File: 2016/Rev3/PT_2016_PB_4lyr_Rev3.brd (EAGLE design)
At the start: 155.7 x 202.7 mm, 166 parts, among them Q1 Q_IRF7437SMD, Q12 2N7002, Q2 2N7002, Q3 Q_IRF7437SMD

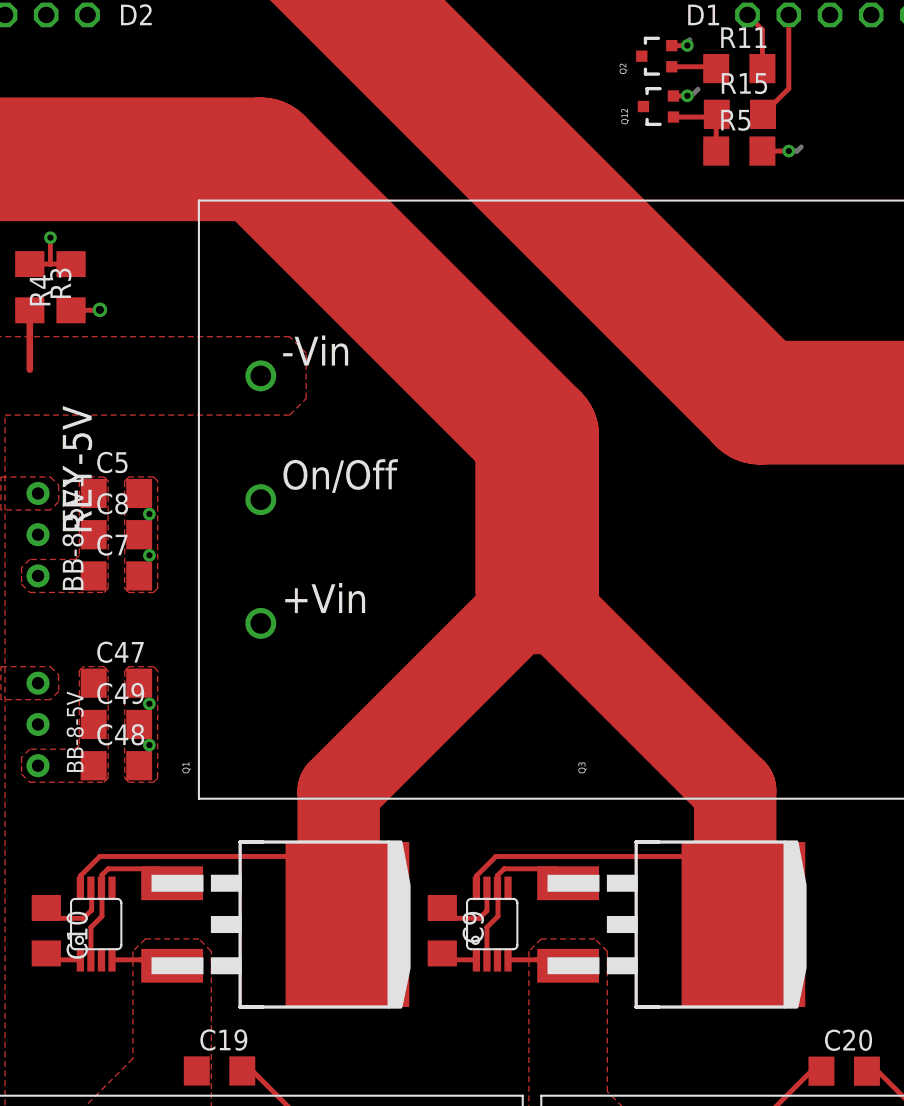
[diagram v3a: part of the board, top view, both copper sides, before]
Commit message: Changed ORing FETs to DPAK
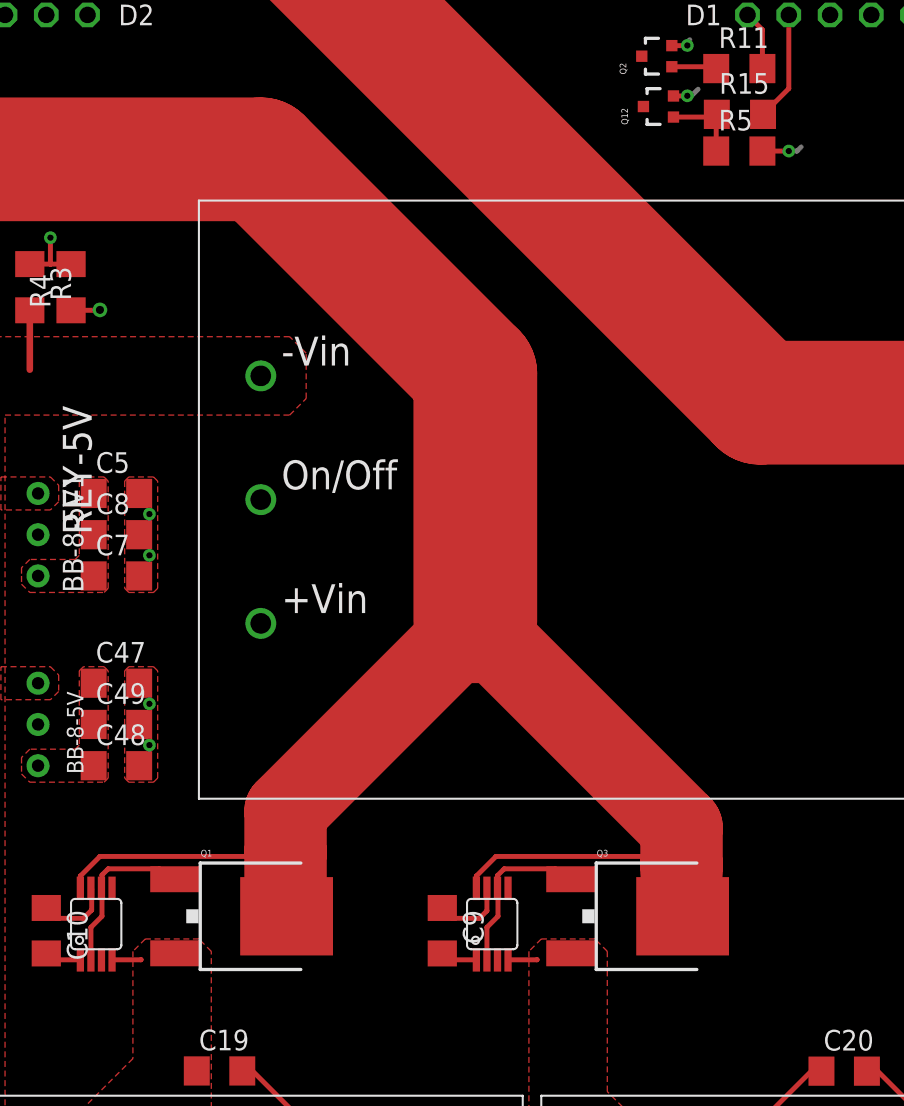
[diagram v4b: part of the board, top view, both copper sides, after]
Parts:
- Q1, Q3: value Q_IRF7437SMD -> MOSFET-NCHANNELFDD8780; device MRDT-2015-PowerBoard:D2PACK -> SparkFun-DiscreteSemi:DPAK
- moved Q1 4.75 mm to (99.8, 97.9)
- moved Q3 4.75 mm to (124.2, 97.9)
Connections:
- net N$1: now also Q3.3; no longer Q3.2
- net N$2: now also Q1.3; no longer Q1.2
- net N$33: now also Q1.4, Q3.4; no longer Q1.TAB, Q3.TAB
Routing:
- net N$33: track 181.3 -> 170.2 mm
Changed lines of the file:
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@@
 <element name="U$9" library="LM74670-Q1" package="LM74670-Q1" value="LM74670-Q1" x="114.046" y="97.536"/>
 <element name="U$13" library="LM74670-Q1" package="LM74670-Q1" value="LM74670-Q1" x="89.662" y="97.536"/>
-<element name="Q1" library="MRDT-2015-PowerBoard" package="D2PACK" value="Q_IRF7437SMD" x="98.552" y="102.489" rot="R270"/>
-<element name="Q3" library="MRDT-2015-PowerBoard" package="D2PACK" value="Q_IRF7437SMD" x="122.936" y="102.489" rot="R270"/>
+<element name="Q1" library="SparkFun-DiscreteSemi" package="DPAK" value="MOSFET-NCHANNELFDD8780" x="99.822" y="97.917" rot="R270">
+<attribute name="PROD_ID" value="TRANS-09984" x="99.822" y="97.917" size="1.778" layer="27" rot="R270" display="off"/>
+</element>
+<element name="Q3" library="SparkFun-DiscreteSemi" package="DPAK" value="MOSFET-NCHANNELFDD8780" x="124.206" y="97.917" rot="R270">
+<attribute name="PROD_ID" value="TRANS-09984" x="124.206" y="97.917" size="1.778" layer="27" rot="R270" display="off"/>
+</element>
 <element name="C9" library="resistor" package="C1206" value="1uF" x="110.998" y="97.028" rot="R270"/>
 <element name="C10" library="resistor" package="C1206" value="1uF" x="86.614" y="97.028" rot="R270"/>
@@
 <wire x1="72.3265" y1="141.70025" x2="79.6925" y2="144.0815" width="0.3048" layer="1"/>
 <wire x1="79.6925" y1="144.0815" x2="79.248" y2="144.526" width="0.3048" layer="1"/>
-<contactref element="Q3" pad="TAB"/>
+<contactref element="Q3" pad="4"/>
 <contactref element="U$9" pad="P$1"/>
-<contactref element="Q1" pad="TAB"/>
+<contactref element="Q1" pad="4"/>
 <contactref element="U$13" pad="P$1"/>
-<wire x1="127" y1="101.6" x2="127.254" y2="101.346" width="0.3048" layer="1"/>
-<wire x1="127.254" y1="101.346" x2="127.254" y2="99.282" width="0.3048" layer="1"/>
-<wire x1="127.254" y1="99.282" x2="129.54" y2="97.409" width="0.3048" layer="1"/>
-<wire x1="99.822" y1="144.526" x2="116.84" y2="127.508" width="7.62" layer="1"/>
-<wire x1="116.84" y1="127.508" x2="116.84" y2="117.856" width="7.62" layer="1"/>
-<wire x1="116.84" y1="117.856" x2="104.616" y2="105.632" width="5.08" layer="1"/>
-<wire x1="114.3" y1="101.6" x2="127" y2="101.6" width="0.3048" layer="1"/>
+<wire x1="99.822" y1="144.526" x2="113.03" y2="131.318" width="7.62" layer="1"/>
+<wire x1="113.03" y1="131.318" x2="113.03" y2="116.078" width="7.62" layer="1"/>
+<wire x1="113.03" y1="116.078" x2="101.346" y2="104.394" width="5.08" layer="1"/>
+<wire x1="101.346" y1="104.394" x2="101.346" y2="101.854" width="5.08" layer="1"/>
+<wire x1="101.346" y1="101.854" x2="101.346" y2="99.06" width="5.08" layer="1"/>
+<wire x1="101.346" y1="99.06" x2="101.41" y2="98.996" width="3.048" layer="1"/>
+<wire x1="101.41" y1="98.996" x2="101.41" y2="97.917" width="3.048" layer="1"/>
+<wire x1="88.712" y1="99.636" x2="88.712" y2="100.396" width="0.3048" layer="1"/>
+<wire x1="88.712" y1="100.396" x2="89.916" y2="101.6" width="0.3048" layer="1"/>
+<wire x1="89.916" y1="101.6" x2="101.092" y2="101.6" width="0.3048" layer="1"/>
+<wire x1="101.092" y1="101.6" x2="101.346" y2="101.854" width="0.3048" layer="1"/>
 <wire x1="113.096" y1="99.636" x2="113.096" y2="100.396" width="0.3048" layer="1"/>
 <wire x1="113.096" y1="100.396" x2="114.3" y2="101.6" width="0.3048" layer="1"/>
-<wire x1="127" y1="101.6" x2="128.778" y2="101.6" width="0.3048" layer="1"/>
-<wire x1="128.778" y1="101.6" x2="129.032" y2="101.346" width="0.3048" layer="1"/>
-<wire x1="129.032" y1="101.346" x2="129.032" y2="105.664" width="5.08" layer="1"/>
-<wire x1="129.032" y1="105.664" x2="116.84" y2="117.856" width="5.08" layer="1"/>
-<wire x1="104.616" y1="105.632" x2="104.616" y2="101.6" width="5.08" layer="1"/>
-<wire x1="104.616" y1="101.6" x2="104.616" y2="97.949" width="5.08" layer="1"/>
-<wire x1="104.616" y1="97.949" x2="105.156" y2="97.409" width="5.08" layer="1"/>
-<wire x1="88.712" y1="99.636" x2="88.712" y2="100.396" width="0.3048" layer="1"/>
-<wire x1="88.712" y1="100.396" x2="89.916" y2="101.6" width="0.3048" layer="1"/>
-<wire x1="89.916" y1="101.6" x2="104.616" y2="101.6" width="0.3048" layer="1"/>
+<wire x1="125.73" y1="100.584" x2="125.73" y2="101.092" width="5.08" layer="1"/>
+<wire x1="125.73" y1="101.092" x2="125.73" y2="103.378" width="5.08" layer="1"/>
+<wire x1="125.73" y1="103.378" x2="113.03" y2="116.078" width="5.08" layer="1"/>
+<wire x1="114.3" y1="101.6" x2="124.968" y2="101.6" width="0.3048" layer="1"/>
+<wire x1="124.968" y1="101.6" x2="124.968" y2="98.743" width="0.3048" layer="1"/>
+<wire x1="124.968" y1="98.743" x2="125.794" y2="97.917" width="0.3048" layer="1"/>
+<wire x1="124.968" y1="101.6" x2="125.222" y2="101.6" width="0.3048" layer="1"/>
+<wire x1="125.222" y1="101.6" x2="125.73" y2="101.092" width="0.3048" layer="1"/>
 </signal>
 <signal name="REC+1">
@@
 <signal name="N$1">
 <contactref element="FINN-12V" pad="8"/>
-<contactref element="Q3" pad="2"/>
+<contactref element="Q3" pad="3"/>
 <contactref element="U$9" pad="P$8"/>
 <contactref element="C20" pad="1"/>
@@
 <signal name="N$2">
 <contactref element="POE-12V" pad="8"/>
-<contactref element="Q1" pad="2"/>
+<contactref element="Q1" pad="3"/>
 <contactref element="U$13" pad="P$8"/>
 <contactref element="C19" pad="1"/>
@@
 <wire x1="114.396" y1="100.426" x2="114.808" y2="100.838" width="0.3048" layer="1"/>
 <wire x1="114.808" y1="100.838" x2="117.963" y2="100.838" width="0.3048" layer="1"/>
-<wire x1="117.963" y1="100.838" x2="118.745" y2="99.949" width="0.3048" layer="1"/>
+<wire x1="117.963" y1="100.838" x2="118.896" y2="100.197" width="0.3048" layer="1"/>
 </signal>
 <signal name="N$5">
@@
 <wire x1="90.043" y1="100.457" x2="90.424" y2="100.838" width="0.3048" layer="1"/>
 <wire x1="90.424" y1="100.838" x2="93.579" y2="100.838" width="0.3048" layer="1"/>
-<wire x1="93.579" y1="100.838" x2="94.361" y2="99.949" width="0.3048" layer="1"/>
+<wire x1="93.579" y1="100.838" x2="94.512" y2="100.197" width="0.3048" layer="1"/>
 <wire x1="89.362" y1="95.236" x2="89.362" y2="97.236" width="0.3048" layer="1"/>
 <wire x1="89.362" y1="97.236" x2="90.043" y2="97.917" width="0.3048" layer="1"/>

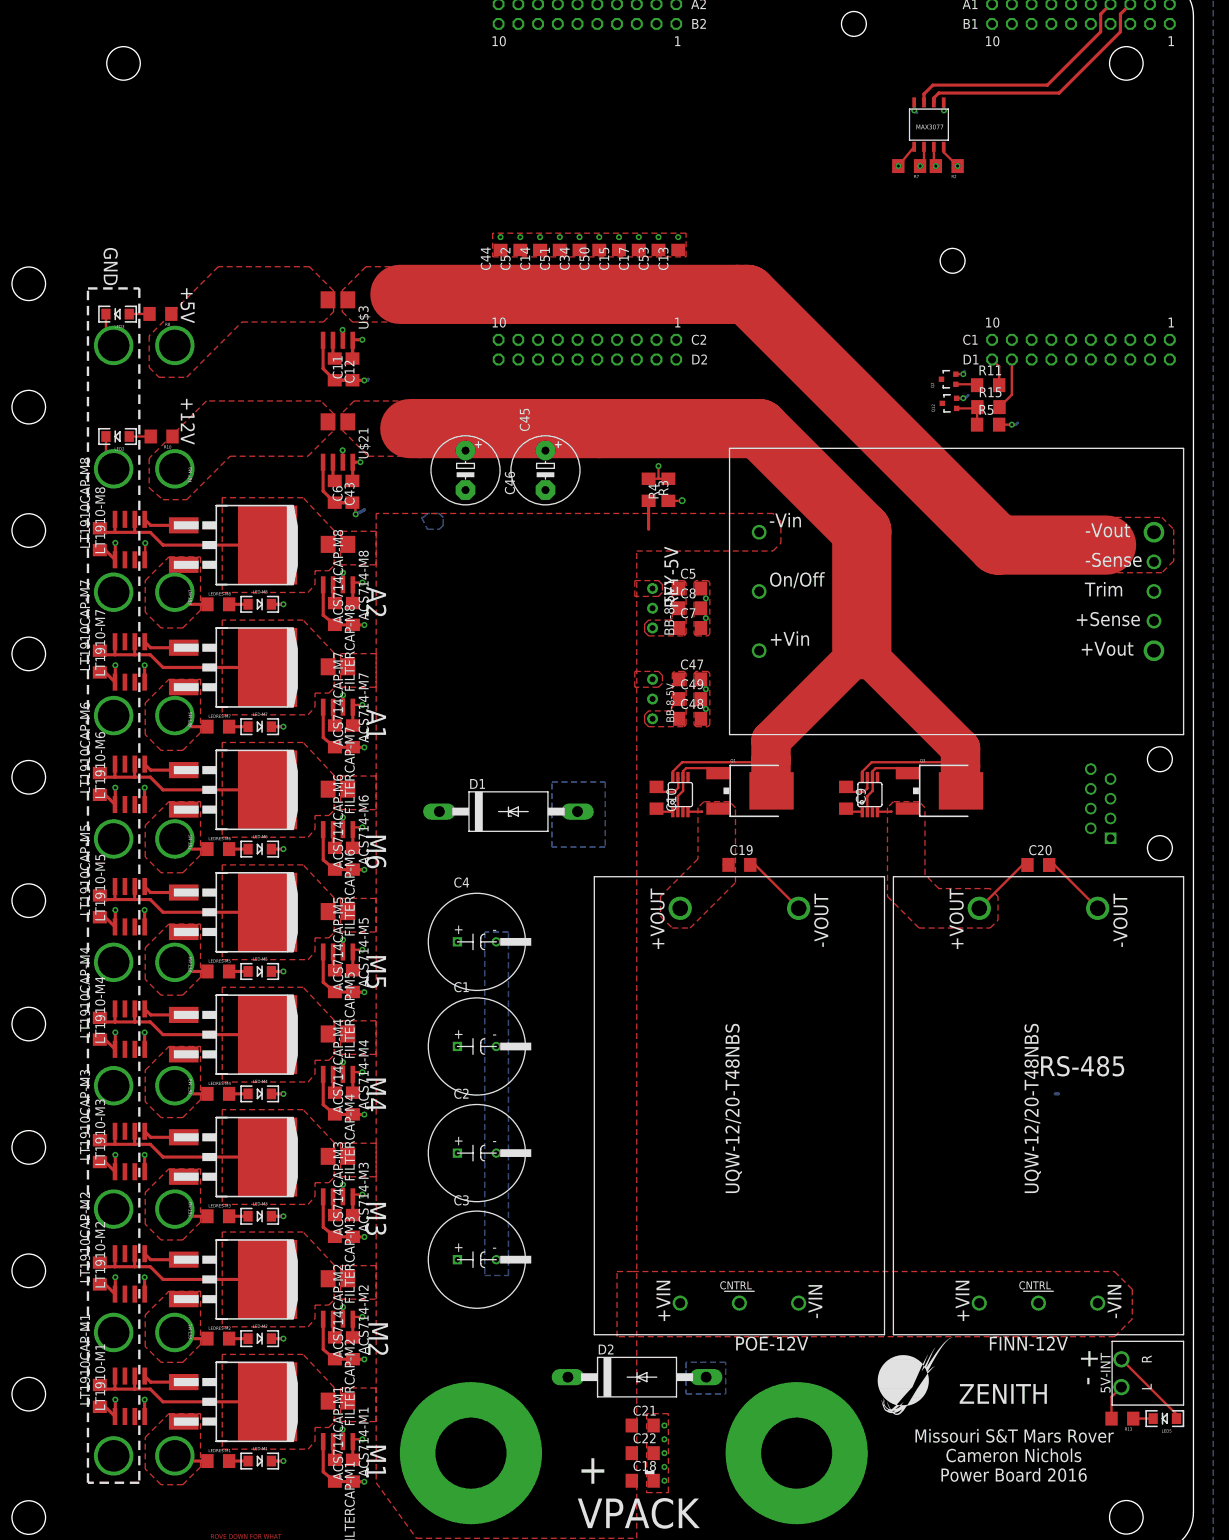
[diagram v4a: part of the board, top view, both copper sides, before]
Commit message: Routed, moved some motor fets over
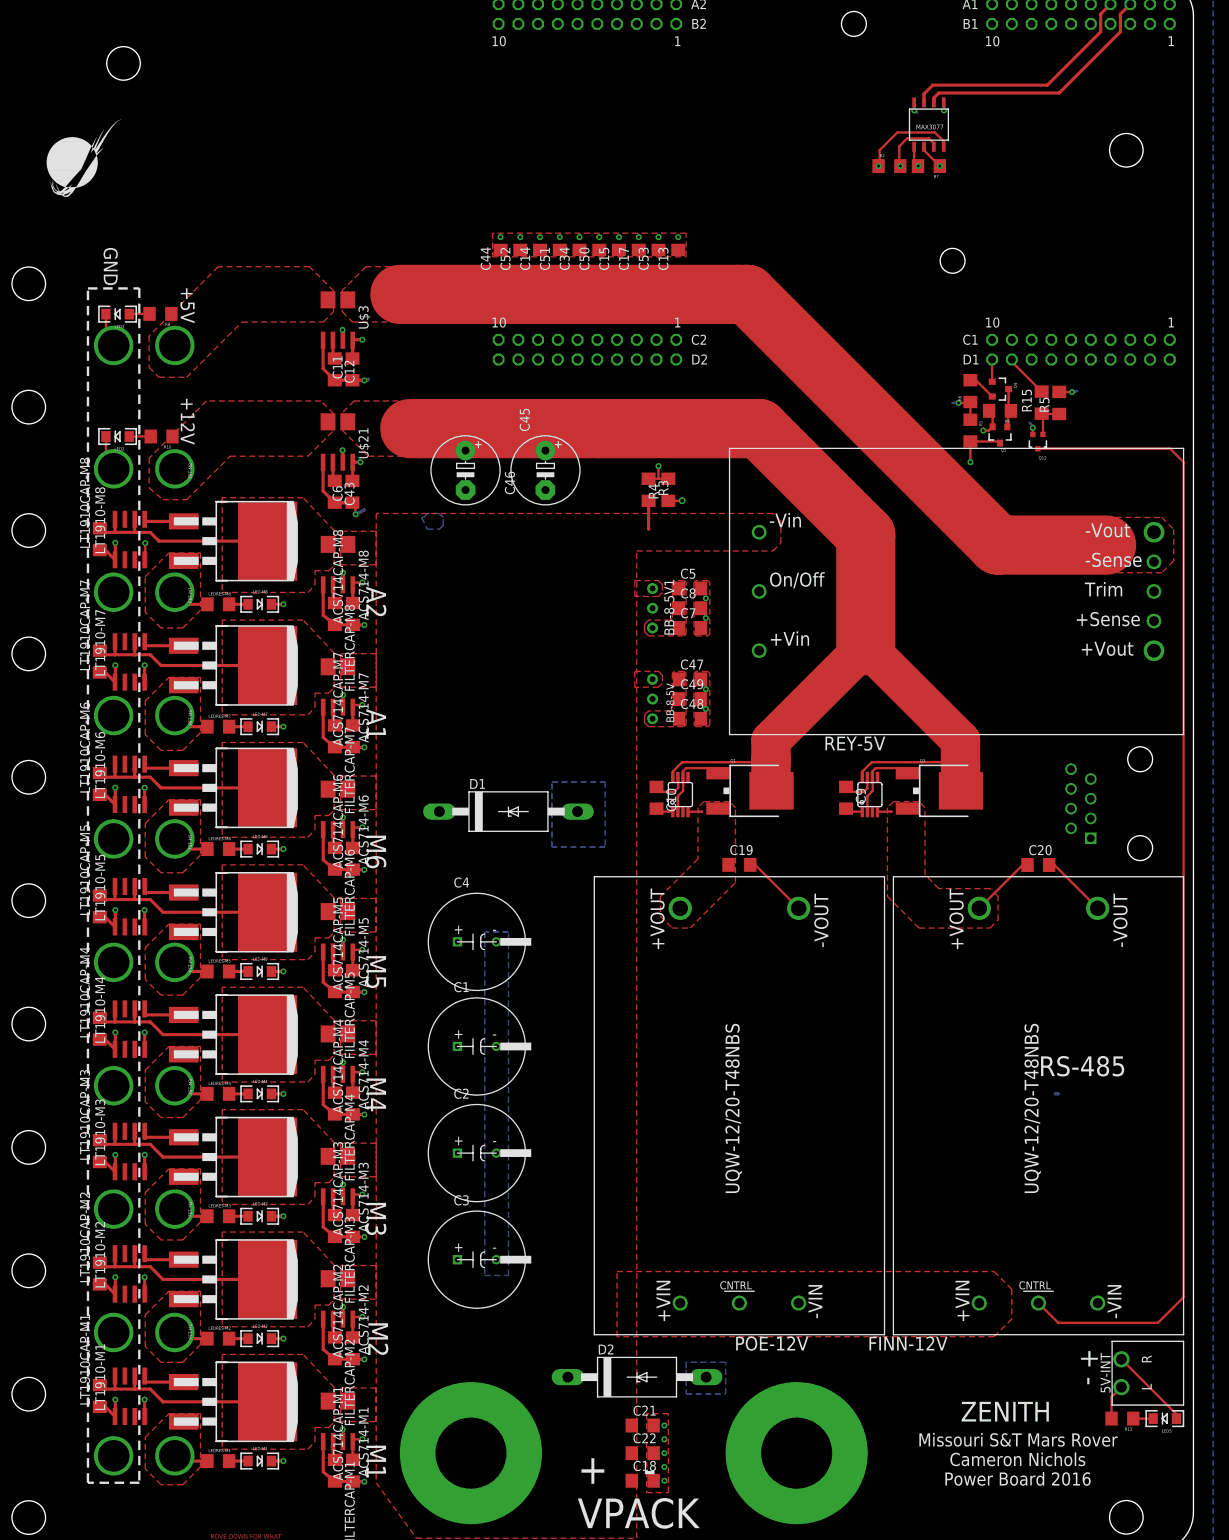
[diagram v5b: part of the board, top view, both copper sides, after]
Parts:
- removed Q2: 2N7002, SparkFun-DiscreteSemi:SOT323
- removed R11: 1k, resistor:R1206
- added Q4: MMBT2222A, SparkFun-DiscreteSemi:SOT23-3
- added Q5: MMBT4403, SparkFun-DiscreteSemi:SOT23-3
- added R1, R6, R9: 120 Ohm, SparkFun-Passives:1206
- moved U$22 189.7 mm to (8.13, 173.5)
- moved Q12 12.4 mm to (135.7, 142.8), turned to 180 degrees
- moved U$11 11.2 mm to (147.1, 180.3)
- moved R5 9.56 mm to (138.4, 147.8), turned to 90 degrees
- moved R2 7.37 mm to (116.6, 178.3), turned to 0 degrees
- moved R15 6.87 mm to (136.2, 147.9), turned to 90 degrees
- moved R7 2.54 mm to (121.7, 178.3)
- moved U$5 2.54 mm to (148.8, 96.3)
- moved FET-M8 0.51 mm to (30.0, 135.1)
- moved FET-M6 0.25 mm to (30.0, 103.4)
- moved FET-M7 0.25 mm to (30.0, 119.1)
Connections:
- removed net N$48: Q2.1, R11.1
- new net N$11: Q4.3, Q5.1, R9.1
- new net N$15: Q4.2, R6.2
- net GND: now also R1.1, R6.1; no longer Q2.2
- net N$43: now also Q5.3, R1.2; no longer Q2.3
- net SIG-5V: now also Q4.1; no longer R11.2
- net V_BATT: now also Q5.2, R9.2
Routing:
- net N$4: track 0.00 -> 188.4 mm
- net N$43: track 0.00 -> 40.6 mm, vias 0 -> 1
- net V_BATT: track 3.66 -> 41.6 mm, vias 0 -> 1
- net TRANS-1: track 104.4 -> 99.0 mm
- net N$11: track 0.00 -> 5.15 mm
- net REC+1: track 117.1 -> 122.1 mm
- net TRANS+1: track 109.2 -> 104.5 mm
- net REC-1: track 116.8 -> 112.2 mm
- net N$15: track 0.00 -> 3.68 mm
- net GND: track 192.7 -> 195.8 mm
- net N$48: track 2.78 -> 0.00 mm
- net SIG-12V: track 6.78 -> 5.72 mm
- net SIG-5V: track 3.68 -> 2.87 mm
- net N$33: track 170.2 -> 170.9 mm

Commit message: Rerouted 5V on/off circuit
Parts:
- added R11: 1k, SparkFun-Passives:1206
- R1, R6, R9: value 120 Ohm -> 1k
- moved Q5 3.23 mm to (133.1, 146.1), turned to 270 degrees
- moved R15 2.92 mm to (137.6, 150.4), turned to 180 degrees
- moved R9 2.75 mm to (128.5, 145.3), turned to 0 degrees
- moved Q12 2.70 mm to (137.7, 144.6)
- moved Q4 2.29 mm to (133.1, 149.6)
- moved R1 2.16 mm to (128.5, 142.7), turned to 0 degrees
- moved R6 2.16 mm to (128.5, 147.8), turned to 0 degrees
- moved R5 0.76 mm to (137.7, 147.8), turned to 180 degrees
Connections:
- net GND: now also R11.1
- net SIG-5V: now also R11.2
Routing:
- net GND: track 195.8 -> 202.8 mm, vias 50 -> 49
- net N$11: track 5.15 -> 9.38 mm
- net N$43: track 40.6 -> 44.7 mm
- net SIG-5V: track 2.87 -> 5.35 mm
- net N$15: track 3.68 -> 2.51 mm
- net SIG-12V: track 5.72 -> 5.13 mm
